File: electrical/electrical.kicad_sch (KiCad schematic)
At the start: 0 parts

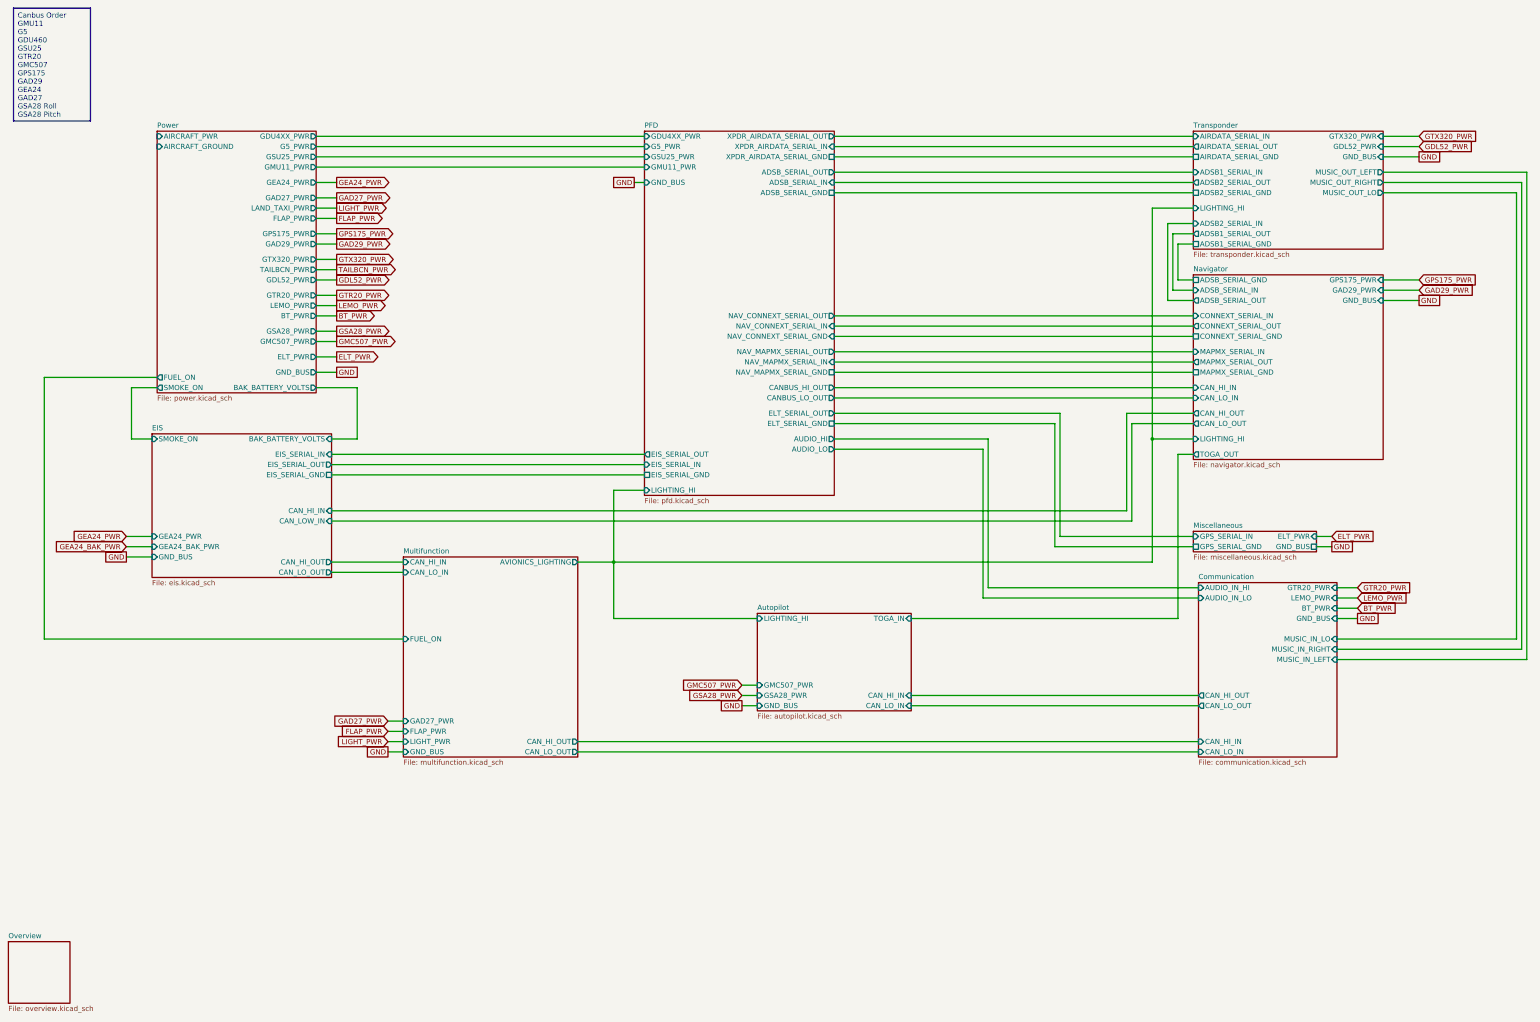
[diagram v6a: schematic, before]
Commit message: Updated canbus diagrams with order for where magnometer and servos will be located. Added yaw servo.
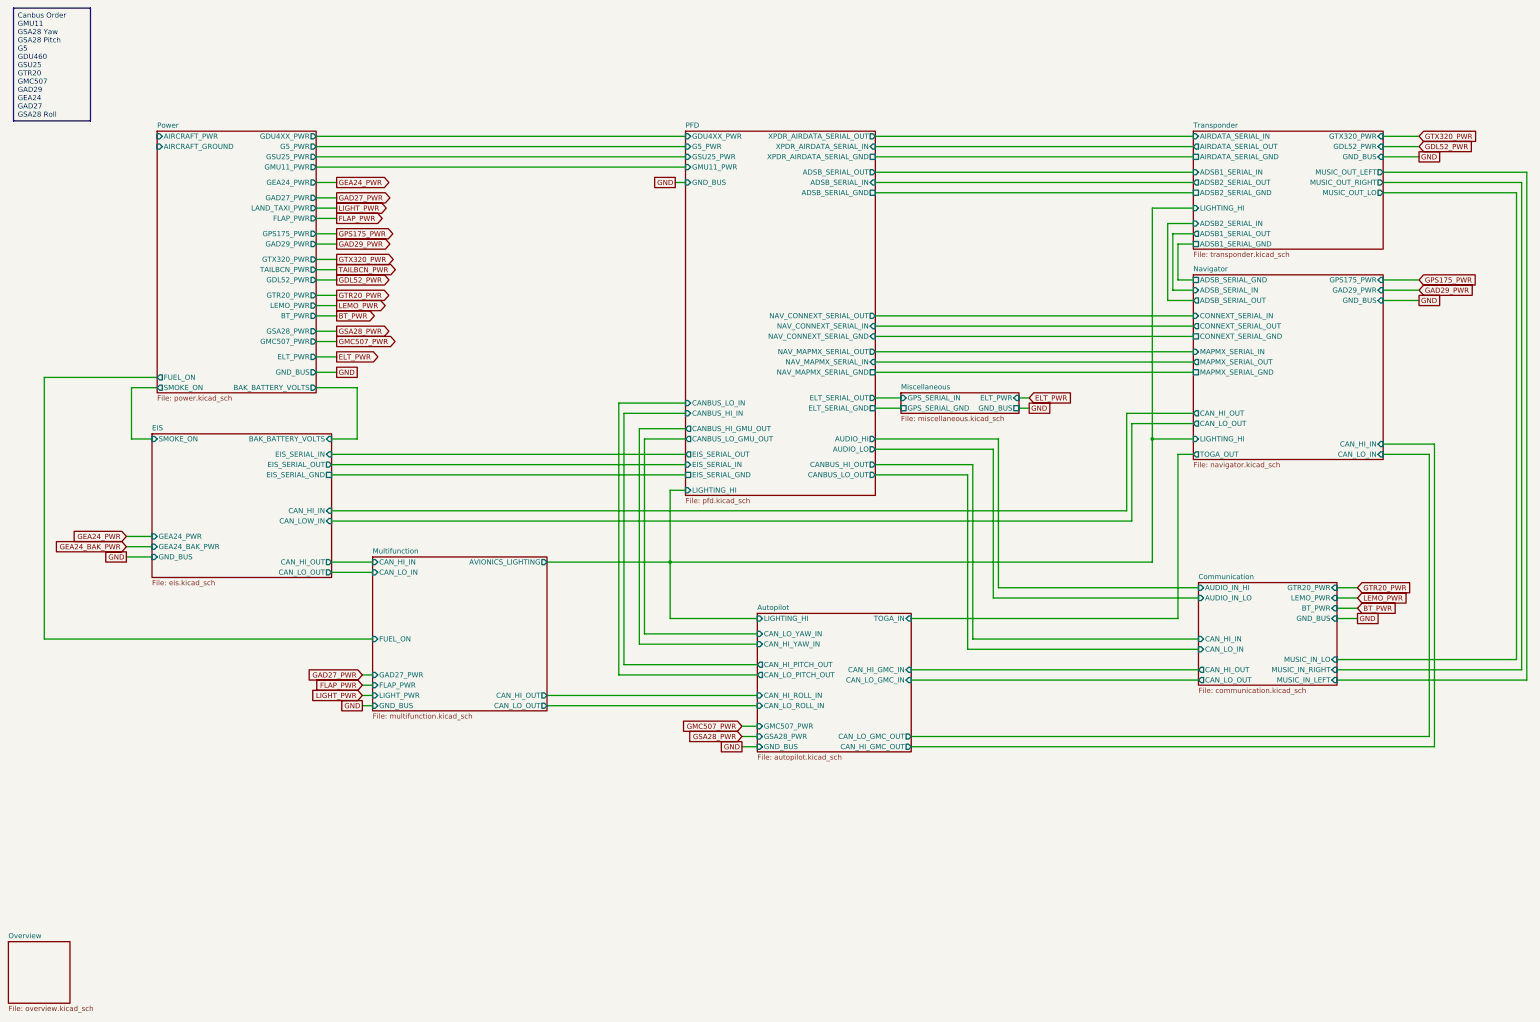
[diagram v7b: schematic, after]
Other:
- sheet Autopilot ports: added CAN_HI_GMC_IN, CAN_HI_GMC_OUT, CAN_HI_PITCH_OUT, CAN_HI_ROLL_IN, CAN_HI_YAW_IN, CAN_LO_GMC_IN, CAN_LO_GMC_OUT, CAN_LO_PITCH_OUT, CAN_LO_ROLL_IN, CAN_LO_YAW_IN; removed CAN_HI_IN, CAN_LO_IN
- sheet PFD ports: added CANBUS_HI_GMU_OUT, CANBUS_HI_IN, CANBUS_LO_GMU_OUT, CANBUS_LO_IN; removed none
